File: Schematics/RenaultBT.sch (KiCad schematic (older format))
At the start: 0 parts

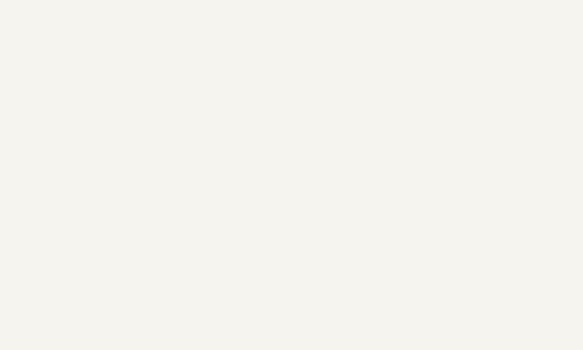
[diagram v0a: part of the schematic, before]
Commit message: Added WM8804 library
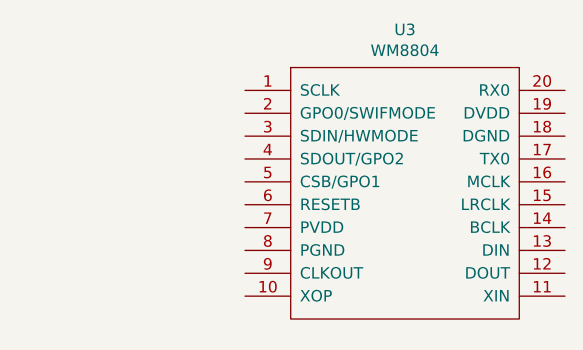
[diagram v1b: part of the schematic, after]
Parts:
- added U3: WM8804, WM8804:WM8804_Breakout_18mm_x_25mm, symbol WM8804:WM8804
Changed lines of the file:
@@
 F6 "GND" I L 1750 1950 50
 $EndSheet
+$Comp
+L WM8804:WM8804 U3
+U 1 1 5CC0CDC5
+P 6000 1500
+F 0 "U3" H 6000 1965 50  0000 C CNN
+F 1 "WM8804" H 6000 1874 50  0000 C CNN
+F 2 "WM8804:WM8804_Breakout_18mm_x_25mm" H 6050 1500 50  0001 C CNN
+F 3 "" H 6050 1500 50  0001 C CNN
+	1    6000 1500
+	1    0    0    -1
+$EndComp
 $EndSCHEMATC

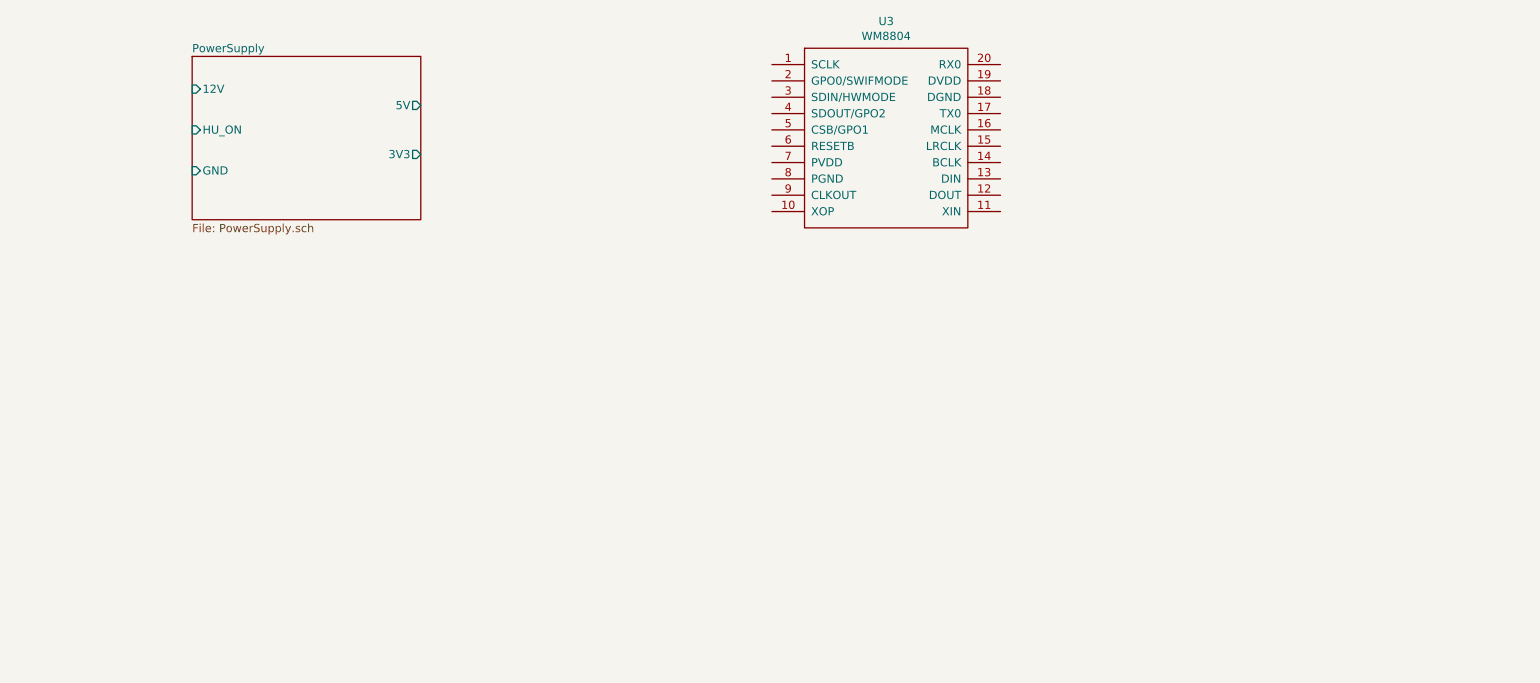
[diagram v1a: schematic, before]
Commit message: Added BT module, HU-CDC interface adapter, I2S to SPDIF converter, SPDIF interface and main controller to the schematics
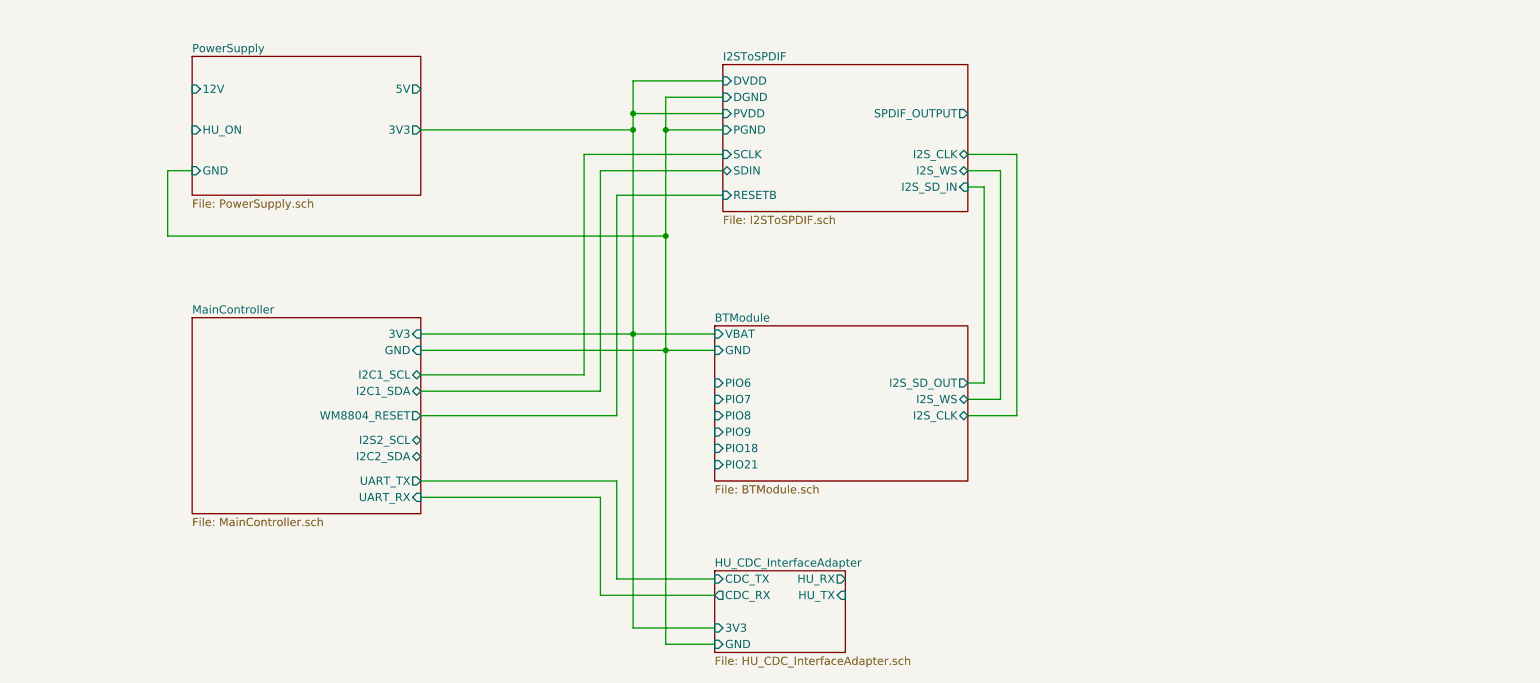
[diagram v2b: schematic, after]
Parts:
- removed U3: WM8804, WM8804:WM8804_Breakout_18mm_x_25mm, symbol WM8804:WM8804
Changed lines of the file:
@@
 $Descr A4 11693 8268
 encoding utf-8
-Sheet 1 2
+Sheet 1 8
 Title ""
 Date ""
@@
 $EndDescr
 $Sheet
-S 1750 1250 1400 1000
+S 1750 1250 1400 850
 U 5CC08323
 F0 "PowerSupply" 50
@@
 F2 "12V" I L 1750 1450 50
 F3 "HU_ON" I L 1750 1700 50
-F4 "5V" O R 3150 1550 50
-F5 "3V3" O R 3150 1850 50
+F4 "5V" O R 3150 1450 50
+F5 "3V3" O R 3150 1700 50
 F6 "GND" I L 1750 1950 50
 $EndSheet
-$Comp
-L WM8804:WM8804 U3
-U 1 1 5CC0CDC5
-P 6000 1500
-F 0 "U3" H 6000 1965 50  0000 C CNN
-F 1 "WM8804" H 6000 1874 50  0000 C CNN
-F 2 "WM8804:WM8804_Breakout_18mm_x_25mm" H 6050 1500 50  0001 C CNN
-F 3 "" H 6050 1500 50  0001 C CNN
-	1    6000 1500
-	1    0    0    -1
-$EndComp
+$Sheet
+S 5000 1300 1500 900
+U 5CCA0E0E
+F0 "I2SToSPDIF" 50
+F1 "I2SToSPDIF.sch" 50
+F2 "DVDD" I L 5000 1400 50
+F3 "PVDD" I L 5000 1600 50
+F4 "PGND" I L 5000 1700 50
+F5 "DGND" I L 5000 1500 50
+F6 "SCLK" I L 5000 1850 50
+F7 "SDIN" B L 5000 1950 50
+F8 "RESETB" I L 5000 2100 50
+F9 "I2S_SD_IN" I R 6500 2050 50
+F10 "I2S_WS" B R 6500 1950 50
+F11 "I2S_CLK" B R 6500 1850 50
+F12 "SPDIF_OUTPUT" O R 6500 1600 50
+$EndSheet
+Wire Wire Line
+	3150 1700 4450 1700
+Wire Wire Line
+	4450 1700 4450 1600
+Wire Wire Line
+	4450 1400 5000 1400
+Wire Wire Line
+	4450 1600 5000 1600
+Wire Wire Line
+	1750 1950 1600 1950
+Wire Wire Line
+	1600 1950 1600 2350
+Wire Wire Line
+	1600 2350 4650 2350
+Wire Wire Line
+	4650 2350 4650 1700
+Wire Wire Line
+	4650 1500 5000 1500
+Wire Wire Line
+	5000 1700 4650 1700
+Connection ~ 4650 1700
+Wire Wire Line
+	4650 1700 4650 1500
+Connection ~ 4450 1600
+Wire Wire Line
+	4450 1600 4450 1400
+$Sheet
+S 4950 2900 1550 950
+U 5CCFC614
+F0 "BTModule" 50
+F1 "BTModule.sch" 50
+F2 "VBAT" I L 4950 2950 50
+F3 "GND" I L 4950 3050 50
+F4 "I2S_SD_OUT" O R 6500 3250 50
+F5 "I2S_WS" B R 6500 3350 50
+F6 "I2S_CLK" B R 6500 3450 50
+F7 "PIO21" I L 4950 3750 50
+F8 "PIO18" I L 4950 3650 50
+F9 "PIO9" I L 4950 3550 50
+F10 "PIO8" I L 4950 3450 50
+F11 "PIO7" I L 4950 3350 50
+F12 "PIO6" I L 4950 3250 50
+$EndSheet
+Wire Wire Line
+	4650 2350 4650 3050
+Connection ~ 4650 2350
+Wire Wire Line
+	6500 3250 6600 3250
+Wire Wire Line
+	6600 3250 6600 2050
+Wire Wire Line
+	6600 2050 6500 2050
+Wire Wire Line
+	6500 1950 6700 1950
+Wire Wire Line
+	6700 1950 6700 3350
+Wire Wire Line
+	6700 3350 6500 3350
+Wire Wire Line
+	6500 3450 6800 3450
+Wire Wire Line
+	6800 3450 6800 1850
+Wire Wire Line
+	6800 1850 6500 1850
+$Sheet
+S 1750 2850 1400 1200
+U 5D07E636
+F0 "MainController" 50
+F1 "MainController.sch" 50
+F2 "I2C1_SCL" B R 3150 3200 50
+F3 "I2C1_SDA" B R 3150 3300 50
+F4 "WM8804_RESET" O R 3150 3450 50
+F5 "I2S2_SCL" B R 3150 3600 50
+F6 "I2C2_SDA" B R 3150 3700 50
+F7 "3V3" I R 3150 2950 50
+F8 "GND" I R 3150 3050 50
+F9 "UART_RX" I R 3150 3950 50
+F10 "UART_TX" O R 3150 3850 50
+$EndSheet
+Connection ~ 4450 1700
+Wire Wire Line
+	4450 2950 4450 1700
+Wire Wire Line
+	3150 3050 4650 3050
+Wire Wire Line
+	4650 3050 4950 3050
+Connection ~ 4650 3050
+Wire Wire Line
+	4950 2950 4450 2950
+Wire Wire Line
+	3150 2950 4450 2950
+Connection ~ 4450 2950
+Wire Wire Line
+	3150 3200 4150 3200
+Wire Wire Line
+	4150 3200 4150 1850
+Wire Wire Line
+	4150 1850 5000 1850
+Wire Wire Line
+	5000 1950 4250 1950
+Wire Wire Line
+	4250 1950 4250 3300
+Wire Wire Line
+	4250 3300 3150 3300
+Wire Wire Line
+	5000 2100 4350 2100
+Wire Wire Line
+	4350 2100 4350 3450
+Wire Wire Line
+	4350 3450 3150 3450
+$Sheet
+S 4950 4400 800  500
+U 5D113669
+F0 "HU_CDC_InterfaceAdapter" 50
+F1 "HU_CDC_InterfaceAdapter.sch" 50
+F2 "GND" I L 4950 4850 50
+F3 "CDC_TX" I L 4950 4450 50
+F4 "HU_RX" O R 5750 4450 50
+F5 "HU_TX" I R 5750 4550 50
+F6 "CDC_RX" O L 4950 4550 50
+F7 "3V3" I L 4950 4750 50
+$EndSheet
+Wire Wire Line
+	3150 3850 4350 3850
+Wire Wire Line
+	4350 3850 4350 4450
+Wire Wire Line
+	4350 4450 4950 4450
+Wire Wire Line
+	4950 4550 4250 4550
+Wire Wire Line
+	4250 4550 4250 3950
+Wire Wire Line
+	4250 3950 3150 3950
+Wire Wire Line
+	4450 2950 4450 4750
+Wire Wire Line
+	4450 4750 4950 4750
+Wire Wire Line
+	4650 3050 4650 4850
+Wire Wire Line
+	4650 4850 4950 4850
 $EndSCHEMATC

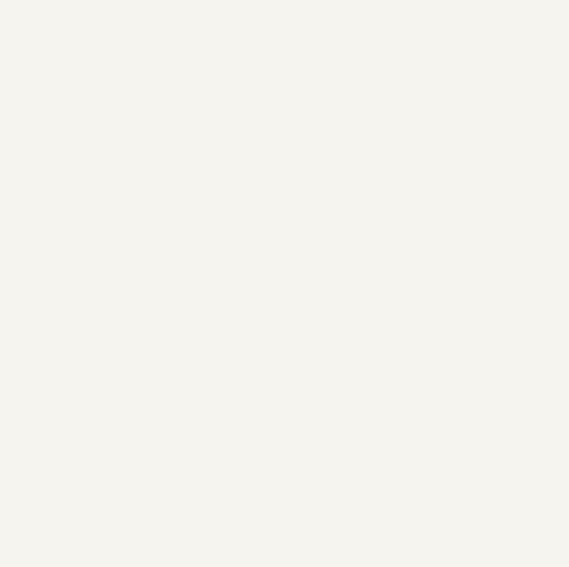
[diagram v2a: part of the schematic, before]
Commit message: Fixed library path errors; added edge-cut for PCB; added screw connector to the schematic
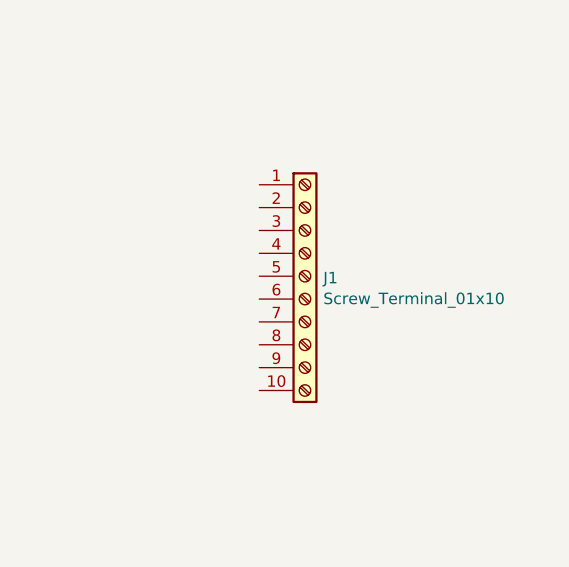
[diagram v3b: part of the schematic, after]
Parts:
- added J1: Screw_Terminal_01x10, symbol Connector:Screw_Terminal_01x10
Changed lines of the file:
@@
 EESchema Schematic File Version 4
 LIBS:RenaultBT-cache
-EELAYER 26 0
+EELAYER 29 0
 EELAYER END
 $Descr A4 11693 8268
@@
 Wire Wire Line
 	4650 4850 4950 4850
+$Comp
+L Connector:Screw_Terminal_01x10 J1
+U 1 1 5D0D7B0A
+P 8850 2900
+F 0 "J1" H 8930 2892 50  0000 L CNN
+F 1 "Screw_Terminal_01x10" H 8930 2801 50  0000 L CNN
+F 2 "" H 8850 2900 50  0001 C CNN
+F 3 "~" H 8850 2900 50  0001 C CNN
+	1    8850 2900
+	1    0    0    -1
+$EndComp
 $EndSCHEMATC

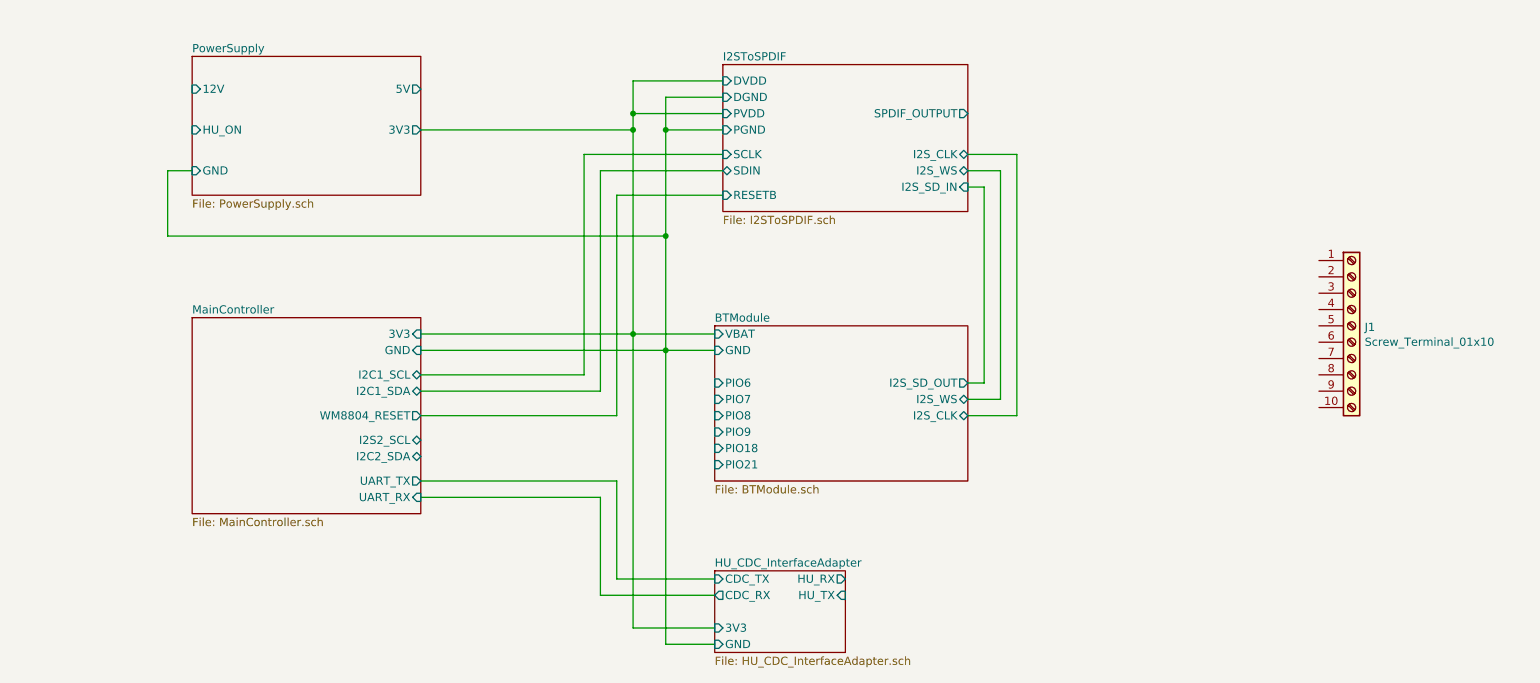
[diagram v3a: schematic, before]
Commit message: Added foorprint for screw terminals; simplified power supply; PCB partial design
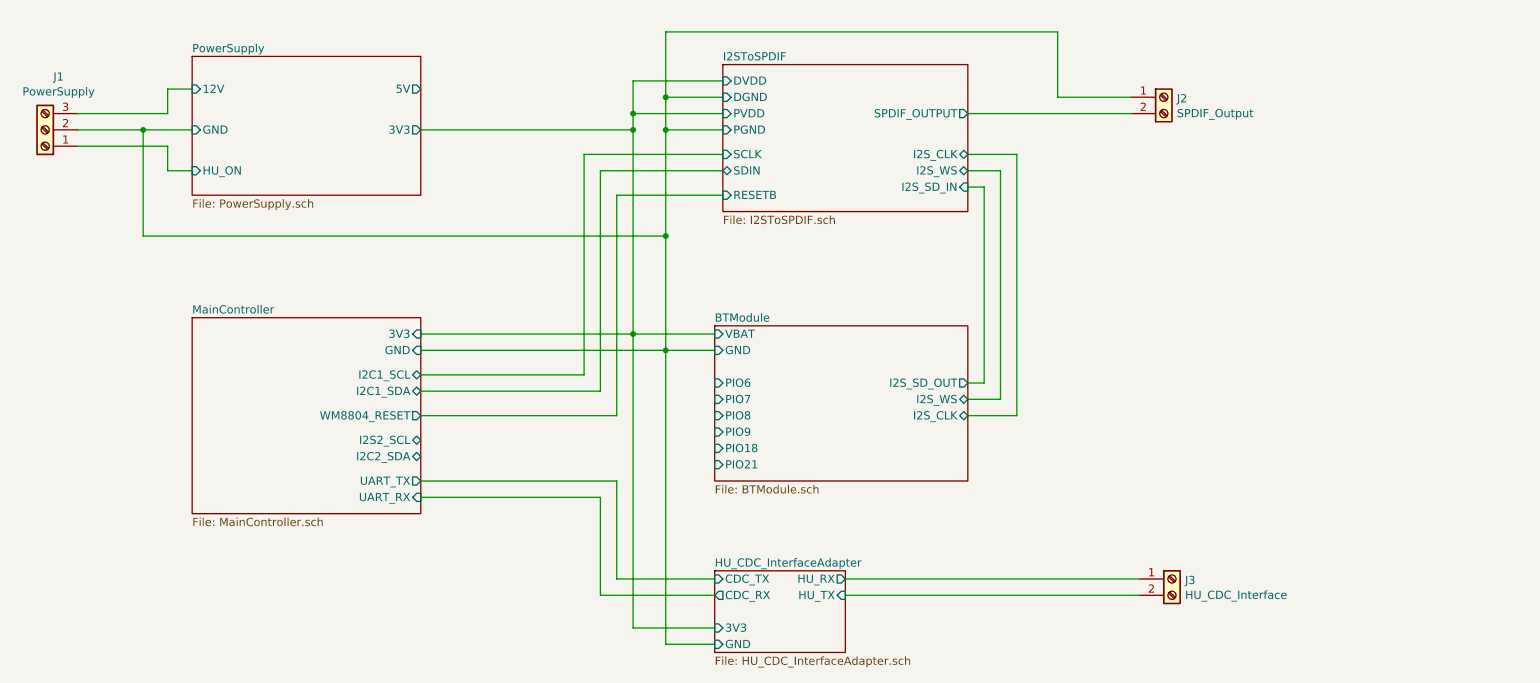
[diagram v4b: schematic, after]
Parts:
- removed J1: Screw_Terminal_01x10, symbol Connector:Screw_Terminal_01x10
- added J1: PowerSupply, ScrewTerminal:ScrewTerminal_3, symbol Connector:Screw_Terminal_01x03
- added J2: SPDIF_Output, ScrewTerminal:ScrewTerminal_2, symbol Connector:Screw_Terminal_01x02
- added J3: HU_CDC_Interface, ScrewTerminal:ScrewTerminal_2, symbol Connector:Screw_Terminal_01x02
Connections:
- net BTModule/GND: now also J1.2 (Pin_2), J2.1 (Pin_1)
- net HU_CDC_InterfaceAdapter/HU_RX: now also J3.1 (Pin_1)
- net HU_CDC_InterfaceAdapter/HU_TX: now also J3.2 (Pin_2)
- net I2SToSPDIF/SPDIF_OUTPUT: now also J2.2 (Pin_2)
- net PowerSupply/12V: now also J1.3 (Pin_3)
- net PowerSupply/HU_ON: now also J1.1 (Pin_1)
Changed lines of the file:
@@
 F1 "PowerSupply.sch" 50
 F2 "12V" I L 1750 1450 50
-F3 "HU_ON" I L 1750 1700 50
+F3 "HU_ON" I L 1750 1950 50
 F4 "5V" O R 3150 1450 50
 F5 "3V3" O R 3150 1700 50
-F6 "GND" I L 1750 1950 50
+F6 "GND" I L 1750 1700 50
 $EndSheet
 $Sheet
@@
 	4450 1600 5000 1600
 Wire Wire Line
-	1750 1950 1600 1950
-Wire Wire Line
-	1600 1950 1600 2350
-Wire Wire Line
-	1600 2350 4650 2350
+	1450 2350 4650 2350
 Wire Wire Line
 	4650 2350 4650 1700
@@
 	4650 4850 4950 4850
 $Comp
-L Connector:Screw_Terminal_01x10 J1
-U 1 1 5D0D7B0A
-P 8850 2900
-F 0 "J1" H 8930 2892 50  0000 L CNN
-F 1 "Screw_Terminal_01x10" H 8930 2801 50  0000 L CNN
-F 2 "" H 8850 2900 50  0001 C CNN
-F 3 "~" H 8850 2900 50  0001 C CNN
-	1    8850 2900
+L Connector:Screw_Terminal_01x03 J1
+U 1 1 5D0CF364
+P 850 1700
+F 0 "J1" H 768 1375 50  0000 C CNN
+F 1 "PowerSupply" H 768 1466 50  0000 C CNN
+F 2 "ScrewTerminal:ScrewTerminal_3" H 850 1700 50  0001 C CNN
+F 3 "~" H 850 1700 50  0001 C CNN
+	1    850  1700
+	-1   0    0    1
+$EndComp
+Wire Wire Line
+	1600 1600 1600 1450
+Wire Wire Line
+	1600 1450 1750 1450
+Wire Wire Line
+	1050 1600 1600 1600
+$Comp
+L Connector:Screw_Terminal_01x02 J2
+U 1 1 5D0D5FA2
+P 7700 1500
+F 0 "J2" H 7780 1492 50  0000 L CNN
+F 1 "SPDIF_Output" H 7780 1401 50  0000 L CNN
+F 2 "ScrewTerminal:ScrewTerminal_2" H 7700 1500 50  0001 C CNN
+F 3 "~" H 7700 1500 50  0001 C CNN
+	1    7700 1500
 	1    0    0    -1
 $EndComp
+Wire Wire Line
+	4650 1500 4650 1100
+Wire Wire Line
+	4650 1100 7050 1100
+Wire Wire Line
+	7050 1100 7050 1500
+Wire Wire Line
+	7050 1500 7500 1500
+Connection ~ 4650 1500
+Wire Wire Line
+	6500 1600 7500 1600
+$Comp
+L Connector:Screw_Terminal_01x02 J3
+U 1 1 5D0DD8D3
+P 7750 4450
+F 0 "J3" H 7830 4442 50  0000 L CNN
+F 1 "HU_CDC_Interface" H 7830 4351 50  0000 L CNN
+F 2 "ScrewTerminal:ScrewTerminal_2" H 7750 4450 50  0001 C CNN
+F 3 "~" H 7750 4450 50  0001 C CNN
+	1    7750 4450
+	1    0    0    -1
+$EndComp
+Wire Wire Line
+	5750 4450 7550 4450
+Wire Wire Line
+	7550 4550 5750 4550
+Wire Wire Line
+	1450 1700 1750 1700
+Wire Wire Line
+	1450 1700 1450 2350
+Wire Wire Line
+	1450 1700 1050 1700
+Connection ~ 1450 1700
+Wire Wire Line
+	1750 1950 1600 1950
+Wire Wire Line
+	1600 1950 1600 1800
+Wire Wire Line
+	1600 1800 1050 1800
 $EndSCHEMATC

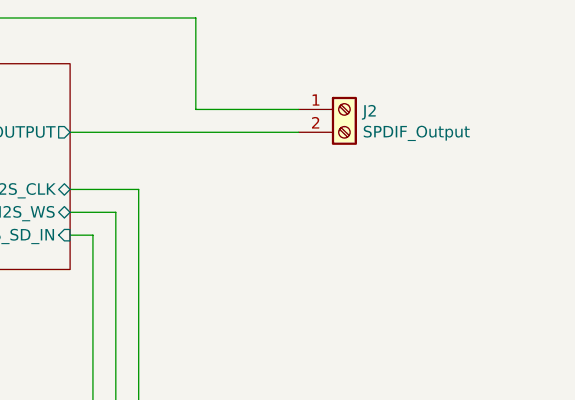
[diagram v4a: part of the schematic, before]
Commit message: Fixed library settings; modified PCB design
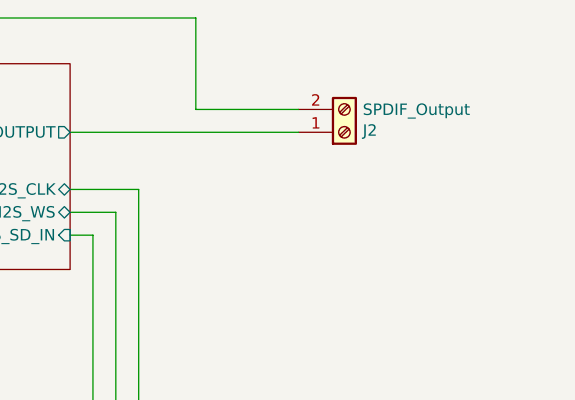
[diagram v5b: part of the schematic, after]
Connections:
- net BTModule/GND: now also J2.2 (Pin_2); no longer J2.1 (Pin_1)
- net I2SToSPDIF/SPDIF_OUTPUT: now also J2.1 (Pin_1); no longer J2.2 (Pin_2)
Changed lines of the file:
@@
 EESchema Schematic File Version 4
 LIBS:RenaultBT-cache
-EELAYER 29 0
+EELAYER 26 0
 EELAYER END
 $Descr A4 11693 8268
@@
 L Connector:Screw_Terminal_01x02 J2
 U 1 1 5D0D5FA2
-P 7700 1500
-F 0 "J2" H 7780 1492 50  0000 L CNN
-F 1 "SPDIF_Output" H 7780 1401 50  0000 L CNN
-F 2 "ScrewTerminal:ScrewTerminal_2" H 7700 1500 50  0001 C CNN
-F 3 "~" H 7700 1500 50  0001 C CNN
-	1    7700 1500
-	1    0    0    -1
+P 7700 1600
+F 0 "J2" H 7780 1592 50  0000 L CNN
+F 1 "SPDIF_Output" H 7780 1501 50  0000 L CNN
+F 2 "ScrewTerminal:ScrewTerminal_2" H 7700 1600 50  0001 C CNN
+F 3 "~" H 7700 1600 50  0001 C CNN
+	1    7700 1600
+	1    0    0    1
 $EndComp
 Wire Wire Line
